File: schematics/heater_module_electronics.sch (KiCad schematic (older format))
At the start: 8 parts, among them P1 Heater PWM Pin, P2 Heating element connector, P3 Heater Thermistor Pin, Q1 MOSFET

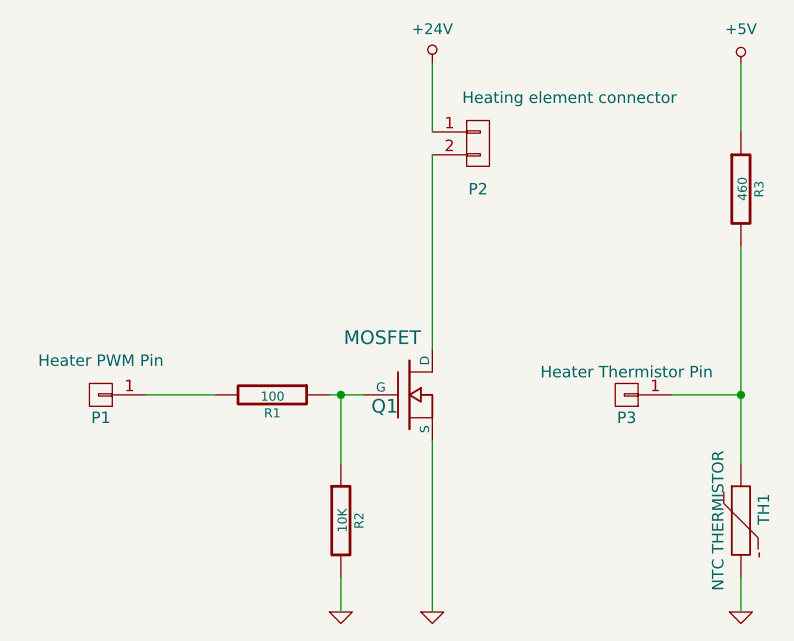
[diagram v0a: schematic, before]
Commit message: Added the flyback diode to schematic
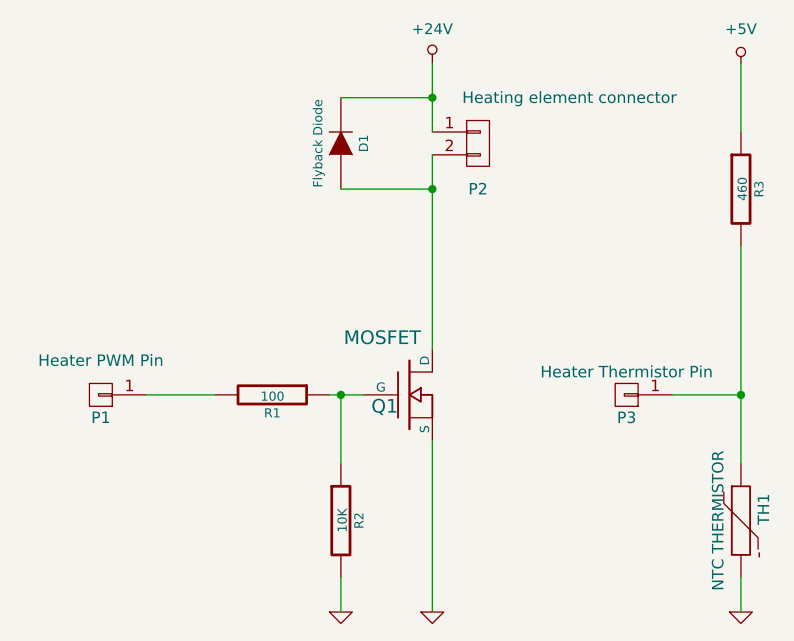
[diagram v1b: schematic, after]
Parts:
- added D1: Flyback Diode, symbol DIODE
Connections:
- net +24V: now also D1.2 (K)
- net at P2.2 (P2), Q1.D: now also D1.1 (A)
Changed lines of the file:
@@
 EESchema Schematic File Version 2
 LIBS:power
+LIBS:74xgxx
+LIBS:74xx
+LIBS:ac-dc
+LIBS:actel
+LIBS:adc-dac
+LIBS:analog_switches
+LIBS:atmel
+LIBS:audio
+LIBS:brooktre
+LIBS:cmos_ieee
+LIBS:cmos4000
+LIBS:conn
+LIBS:contrib
+LIBS:cypress
+LIBS:dc-dc
+LIBS:device
+LIBS:digital-audio
+LIBS:display
+LIBS:dsp
+LIBS:elec-unifil
+LIBS:ftdi
+LIBS:gennum
+LIBS:graphic
+LIBS:hc11
+LIBS:intel
+LIBS:interface
+LIBS:ir
+LIBS:linear
+LIBS:logo
+LIBS:memory
+LIBS:microchip_pic10mcu
+LIBS:microchip_pic12mcu
+LIBS:microchip_pic16mcu
+LIBS:microchip_pic18mcu
+LIBS:microchip
+LIBS:microchip1
+LIBS:microcontrollers
+LIBS:motorola
+LIBS:msp430
+LIBS:noname-cache
+LIBS:nxp_armmcu
+LIBS:opto
+LIBS:philips
+LIBS:powerint
+LIBS:pspice
+LIBS:references
+LIBS:regul
+LIBS:relays
+LIBS:rfcom
+LIBS:sensors
+LIBS:siliconi
+LIBS:special
+LIBS:stm8
+LIBS:stm32
+LIBS:supertex
+LIBS:texas
+LIBS:transf
+LIBS:transistors
+LIBS:ttl_ieee
+LIBS:valves
+LIBS:video
+LIBS:xilinx
 LIBS:heater_module_electronics-cache
 EELAYER 24 0
@@
 Wire Wire Line
 	5350 2400 5350 2700
+$Comp
+L DIODE D1
+U 1 1 540A2799
+P 4950 2750
+F 0 "D1" H 4950 2650 40  0000 C CNN
+F 1 "Flyback Diode" H 4950 2850 40  0000 C CNN
+F 2 "" H 4950 2750 60  0000 C CNN
+F 3 "" H 4950 2750 60  0000 C CNN
+	1    4950 2750
+	0    -1   -1   0
+$EndComp
+Wire Wire Line
+	4950 2550 5350 2550
+Connection ~ 5350 2550
+Wire Wire Line
+	4950 2950 5350 2950
+Connection ~ 5350 2950
 $EndSCHEMATC
